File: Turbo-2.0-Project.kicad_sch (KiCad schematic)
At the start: 1 part, among them J1 Conn_01x02

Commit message: Update es32
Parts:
- added U1: ESP32-C3-WROOM-02, RF_Module:ESP32-C3-WROOM-02, symbol RF_Module:ESP32-C3-WROOM-02
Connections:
- new net: U1.19 (GND), U1.9 (GND)
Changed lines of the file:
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@@
+	)
+	(symbol
+		(lib_id "RF_Module:ESP32-C3-WROOM-02")
+		(at 102.87 60.96 0)
+		(unit 1)
+		(exclude_from_sim no)
+		(in_bom yes)
+		(on_board yes)
+		(dnp no)
+		(fields_autoplaced yes)
+		(property "Reference" "U1"
+			(at 105.0133 35.56 0)
+			(effects
+				(font
+					(size 1.27 1.27)
+				)
+				(justify left)
+			)
+		)
+		(property "Value" "ESP32-C3-WROOM-02"
+			(at 105.0133 38.1 0)
+			(effects
+				(font
+					(size 1.27 1.27)
+				)
+				(justify left)
+			)
+		)
+		(property "Footprint" "RF_Module:ESP32-C3-WROOM-02"
+			(at 102.87 60.325 0)
+			(effects
+				(font
+					(size 1.27 1.27)
+				)
+				(hide yes)
+			)
+		)
+		(property "Datasheet" "https://www.espressif.com/sites/default/files/documentation/esp32-c3-wroom-02_datasheet_en.pdf"
+			(at 102.87 60.325 0)
+			(effects
+				(font
+					(size 1.27 1.27)
+				)
+				(hide yes)
+			)
+		)
+		(property "Description" "802.11 b/g/n Wi­Fi and Bluetooth 5 module, ESP32­C3 SoC, RISC­V microprocessor, On-board antenna"
+			(at 102.87 60.325 0)
+			(effects
+				(font
+					(size 1.27 1.27)
+				)
+				(hide yes)
+			)
+		)
+		(pin "7"
+		)
+		(pin "4"
+		)
+		(pin "3"
+		)
+		(pin "19"
+		)
+		(pin "17"
+		)
+		(pin "9"
+		)
+		(pin "11"
+		)
+		(pin "12"
+		)
+		(pin "2"
+		)
+		(pin "1"
+		)
+		(pin "6"
+		)
+		(pin "5"
+		)
+		(pin "14"
+		)
+		(pin "13"
+		)
+		(pin "15"
+		)
+		(pin "18"
+		)
+		(pin "16"
+		)
+		(pin "8"
+		)
+		(pin "10"
+		)
+		(instances
+			(project ""
+				(path "/aed3ed38-84bd-46b2-8591-0345416ed942"
+					(reference "U1")
+					(unit 1)
+				)
+			)
+		)
 	)
 	(symbol

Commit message: Updat4re
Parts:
- added M1: Motor_Servo, symbol Motor:Motor_Servo
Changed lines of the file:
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@@
+	)
+	(symbol
+		(lib_id "Motor:Motor_Servo")
+		(at 143.51 104.14 0)
+		(unit 1)
+		(exclude_from_sim no)
+		(in_bom yes)
+		(on_board yes)
+		(dnp no)
+		(fields_autoplaced yes)
+		(property "Reference" "M1"
+			(at 152.4 102.4368 0)
+			(effects
+				(font
+					(size 1.27 1.27)
+				)
+				(justify left)
+			)
+		)
+		(property "Value" "Motor_Servo"
+			(at 152.4 104.9768 0)
+			(effects
+				(font
+					(size 1.27 1.27)
+				)
+				(justify left)
+			)
+		)
+		(property "Footprint" ""
+			(at 143.51 108.966 0)
+			(effects
+				(font
+					(size 1.27 1.27)
+				)
+				(hide yes)
+			)
+		)
+		(property "Datasheet" "http://forums.parallax.com/uploads/attachments/46831/74481.png"
+			(at 143.51 108.966 0)
+			(effects
+				(font
+					(size 1.27 1.27)
+				)
+				(hide yes)
+			)
+		)
+		(property "Description" "Servo Motor (Futaba, HiTec, JR connector)"
+			(at 143.51 104.14 0)
+			(effects
+				(font
+					(size 1.27 1.27)
+				)
+				(hide yes)
+			)
+		)
+		(pin "2"
+		)
+		(pin "3"
+		)
+		(pin "1"
+		)
+		(instances
+			(project ""
+				(path "/aed3ed38-84bd-46b2-8591-0345416ed942"
+					(reference "M1")
+					(unit 1)
+				)
+			)
+		)
 	)
 	(symbol

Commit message: duplicate
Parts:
- added J2: Conn_01x02, symbol Connector_Generic:Conn_01x02
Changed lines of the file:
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@@
+	)
+	(symbol
+		(lib_id "Connector_Generic:Conn_01x02")
+		(at 146.05 68.58 0)
+		(unit 1)
+		(exclude_from_sim no)
+		(in_bom yes)
+		(on_board yes)
+		(dnp no)
+		(fields_autoplaced yes)
+		(property "Reference" "J2"
+			(at 148.59 68.5799 0)
+			(effects
+				(font
+					(size 1.27 1.27)
+				)
+				(justify left)
+			)
+		)
+		(property "Value" "Conn_01x02"
+			(at 148.59 71.1199 0)
+			(effects
+				(font
+					(size 1.27 1.27)
+				)
+				(justify left)
+			)
+		)
+		(property "Footprint" ""
+			(at 146.05 68.58 0)
+			(effects
+				(font
+					(size 1.27 1.27)
+				)
+				(hide yes)
+			)
+		)
+		(property "Datasheet" "~"
+			(at 146.05 68.58 0)
+			(effects
+				(font
+					(size 1.27 1.27)
+				)
+				(hide yes)
+			)
+		)
+		(property "Description" "Generic connector, single row, 01x02, script generated (kicad-library-utils/schlib/autogen/connector/)"
+			(at 146.05 68.58 0)
+			(effects
+				(font
+					(size 1.27 1.27)
+				)
+				(hide yes)
+			)
+		)
+		(pin "2"
+		)
+		(pin "1"
+		)
+		(instances
+			(project "Turbo-2.0-Project"
+				(path "/aed3ed38-84bd-46b2-8591-0345416ed942"
+					(reference "J2")
+					(unit 1)
+				)
+			)
+		)
 	)
 	(symbol

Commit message: WHats up
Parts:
- removed J1, J2: Conn_01x02, symbol Connector_Generic:Conn_01x02
- removed M1: Motor_Servo, symbol Motor:Motor_Servo
- removed U1: ESP32-C3-WROOM-02, RF_Module:ESP32-C3-WROOM-02, symbol RF_Module:ESP32-C3-WROOM-02
- added J1, J4, J5: Conn_01x06, symbol Connector_Generic:Conn_01x06
- added J2, J3: Conn_01x04, symbol Connector_Generic:Conn_01x04
- added U1: ~, symbol Turbo_Custom_Library:ESP32S3_Mini_Zero
- added U2: ~, symbol Turbo_Custom_Library:DRV8833_Motor_Driver
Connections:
- new net: J2.4 (Pin_4), U1. (7)

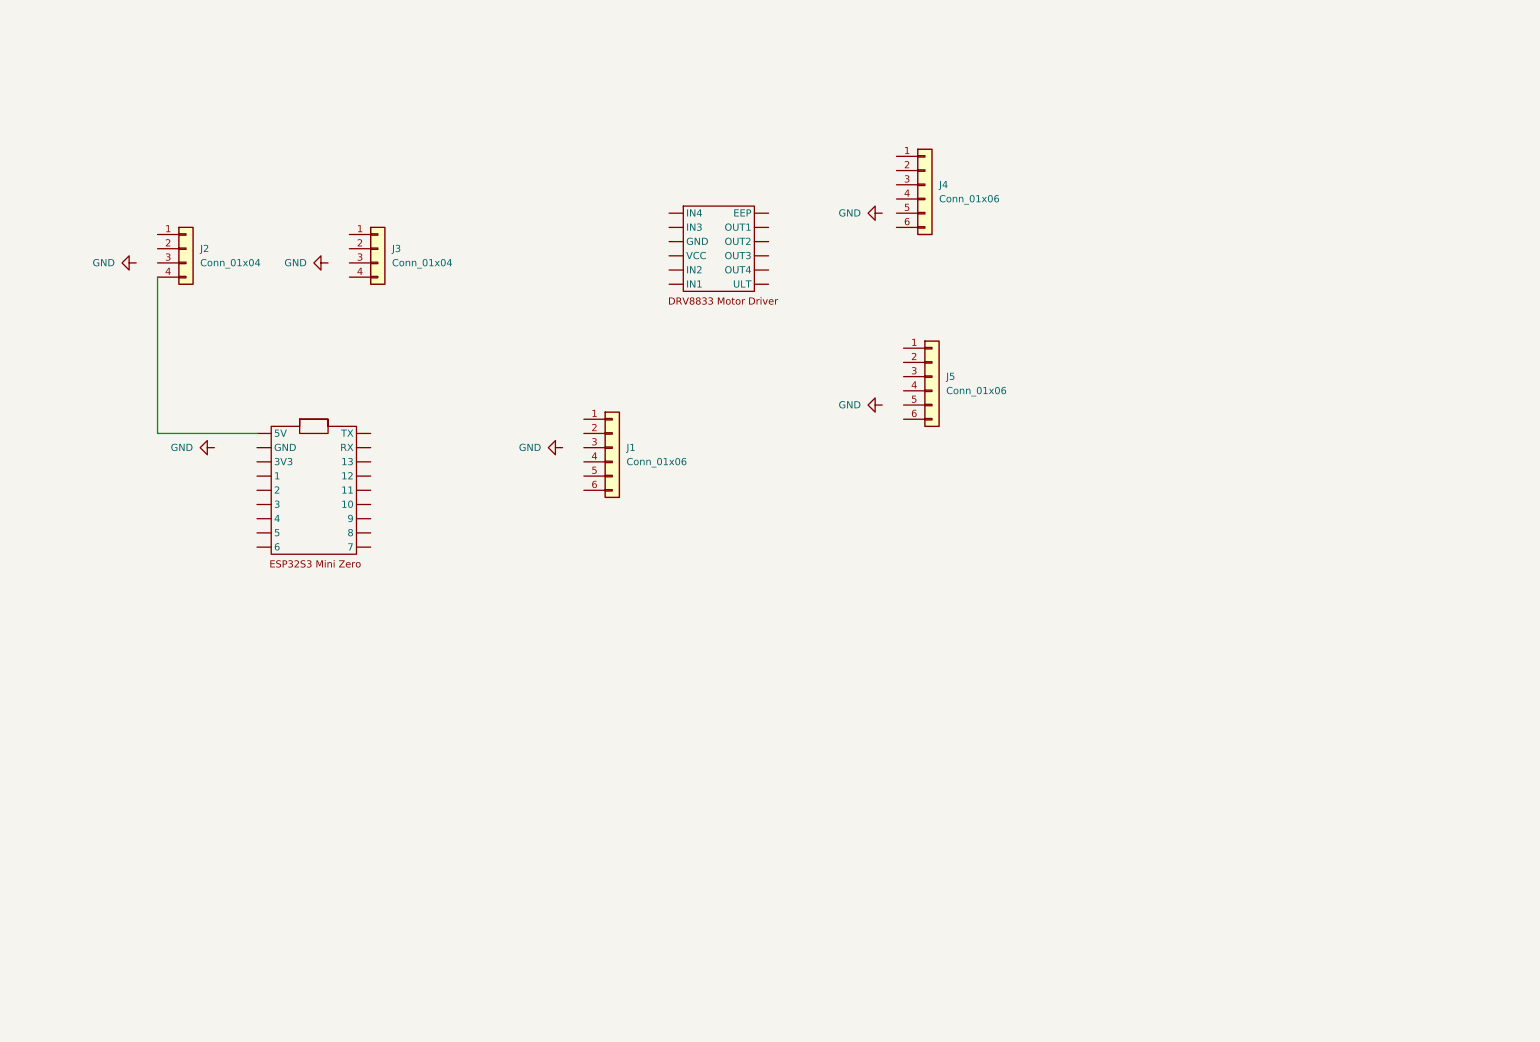
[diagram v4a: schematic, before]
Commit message: Completed Sensor and Emitter Circuitry
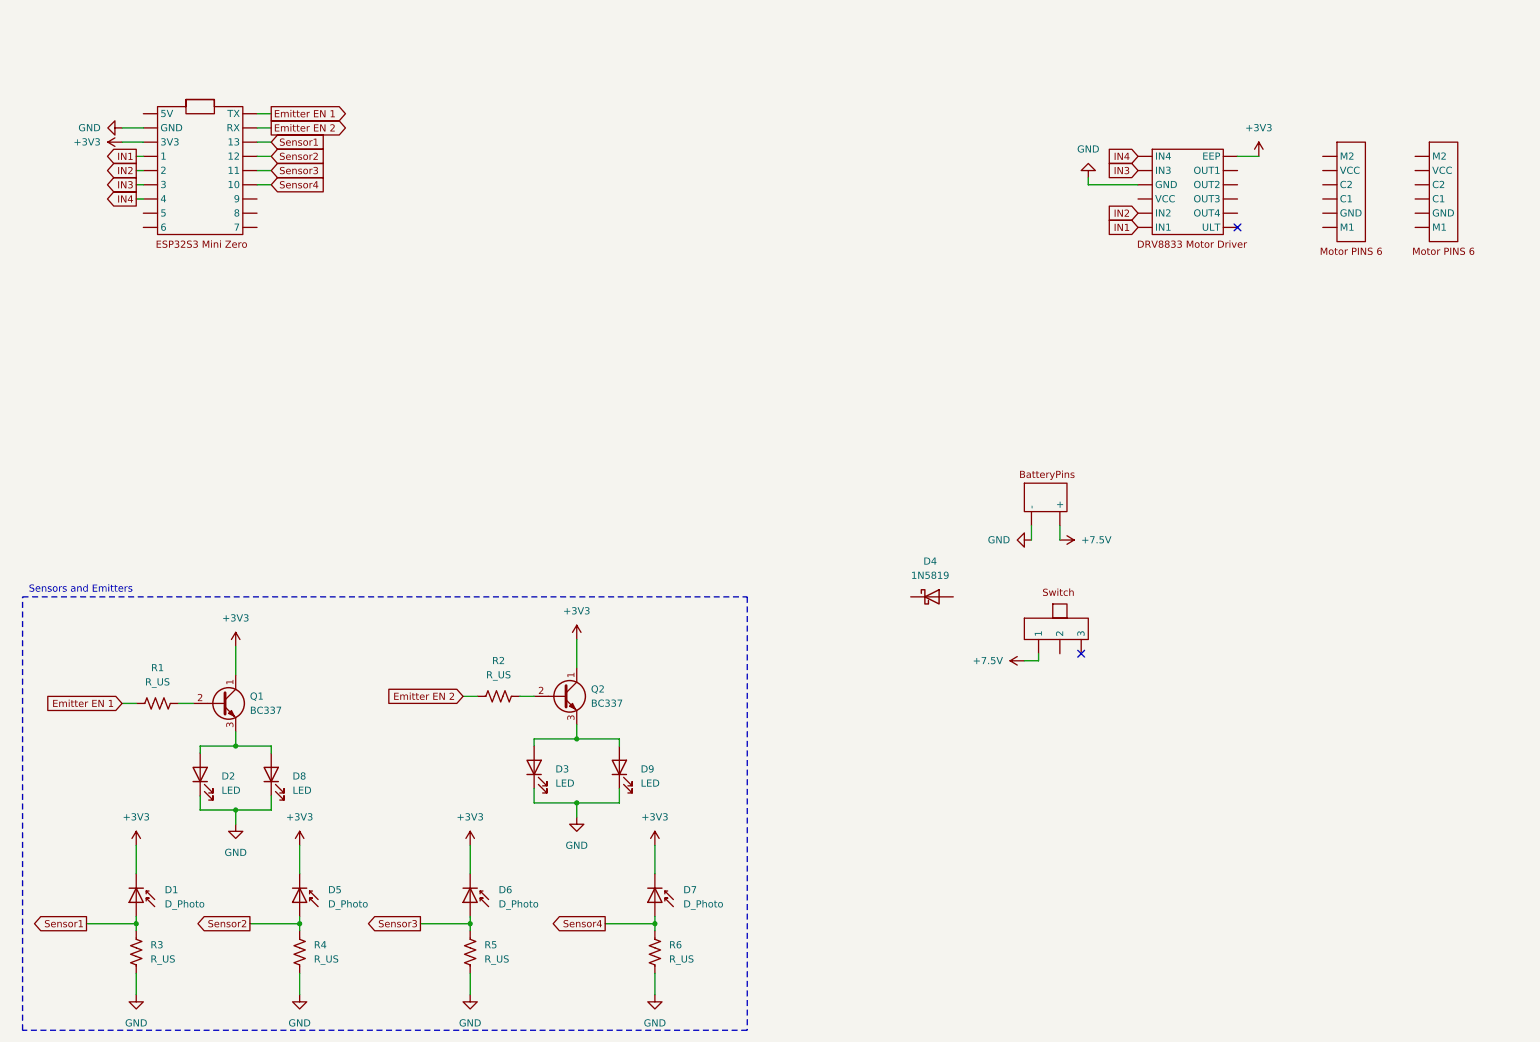
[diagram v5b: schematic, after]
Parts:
- removed J1, J4, J5: Conn_01x06, symbol Connector_Generic:Conn_01x06
- removed J2, J3: Conn_01x04, symbol Connector_Generic:Conn_01x04
- added D1, D5, D6, D7: D_Photo, symbol Device:D_Photo
- added D2, D3, D8, D9: LED, symbol Device:LED
- added D4: 1N5819, Diode_THT:D_DO-41_SOD81_P10.16mm_Horizontal, symbol Diode:1N5819
- added Q1, Q2: BC337, Package_TO_SOT_THT:TO-92_Inline, symbol Transistor_BJT:BC337
- added R1, R2, R3, R4, R5, R6: R_US, symbol Device:R_US
- added U3, U4: ~, symbol Turbo_Custom_Library:MotorPin6
- added U5: ~, symbol Turbo_Custom_Library:Battery
- added U6: ~, symbol Turbo_Custom_Library:Switch
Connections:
- net GND: now also U1. (7), U2. (ULT), D2.1 (K), D3.1 (K), D8.1 (K), D9.1 (K), R3.2, R4.2, R5.2, R6.2, U5. (+)
- net Sensor4: now reaches U1. (7)
- net Sensor4: now also D7.2 (A), R6.1
- net IN4: now reaches U2. (ULT)
- net IN4: now also U1. (7)
- new net: D2.2 (A), D8.2 (A), Q1.3 (E)
- new net: Q1.2 (B), R1.2
- new net: Q2.2 (B), R2.2
- new net: D3.2 (A), D9.2 (A), Q2.3 (E)
- new net +3V3: D1.1 (K), D5.1 (K), D6.1 (K), D7.1 (K), Q1.1 (C), Q2.1 (C), U1. (7), U2. (ULT)
- new net +7.5V: U5. (+), U6. (3)
- new net Emitter EN 1: R1.1, U1. (7)
- new net Emitter EN 2: R2.1, U1. (7)
- new net IN1: U1. (7), U2. (ULT)
- new net IN2: U1. (7), U2. (ULT)
- new net IN3: U1. (7), U2. (ULT)
- new net Sensor1: D1.2 (A), R3.1, U1. (7)
- new net Sensor2: D5.2 (A), R4.1, U1. (7)
- new net Sensor3: D6.2 (A), R5.1, U1. (7)
- no-connect marks 0 -> 2
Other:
- note added: "Sensors and Emitters"

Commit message: Wired Everything Up
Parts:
- added U7, U8: ~, symbol Turbo_Custom_Library:Step_down
- added U9: ~, symbol Turbo_Custom_Library:BNO085_IMU
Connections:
- net +3V3: now also U3. (M1), U4. (M1)
- net GND: now also U3. (M1), U4. (M1), U6. (3), U7. (Vo+), U8. (Vo+)
- net OUT2: now reaches U3. (M1)
- net OUT2: now also U2. (ULT), U4. (M1)
- net OUT4: now reaches U2. (ULT)
- net at D4.1 (K): now also U1. (7)
- net +5V: now reaches D4.2 (A)
- net +5V: now also U7. (Vo+)
- new net: U6. (3), U7. (Vo+), U8. (Vo+)
- new net +6V: U2. (ULT), U8. (Vo+)
- new net Motor1 C1: U1. (7), U3. (M1)
- new net Motor1 C2: U1. (7), U3. (M1)
- new net Motor2 C1: U1. (7), U4. (M1)
- new net Motor2 C2: U1. (7), U4. (M1)
- new net OUT1: U2. (ULT), U3. (M1), U4. (M1)
- new net OUT3: U2. (ULT)
- no-connect marks 2 -> 1
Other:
- note added: "Microcontroller"
- note added: "Motors and Driver"
- note added: "Power Circuitry"
- moved on the sheet: D1, D2, D3, D4, D5, D6, D7, D8, D9, Q1, Q2, R1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

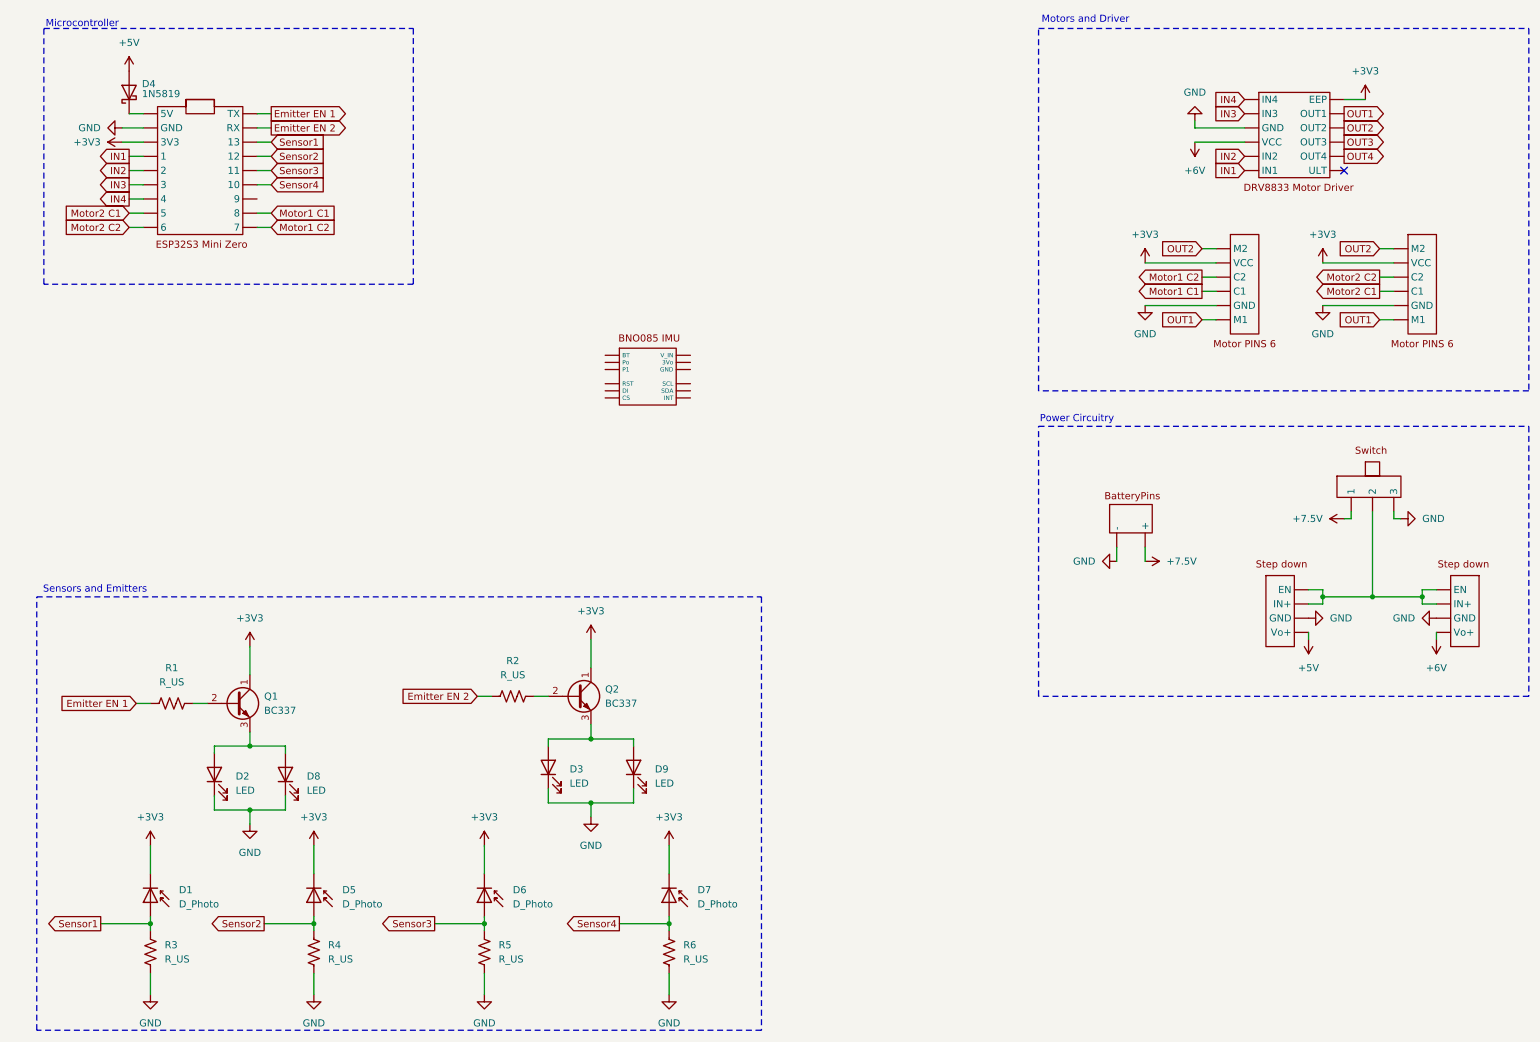
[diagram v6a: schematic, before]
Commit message: Added IMU to schematic
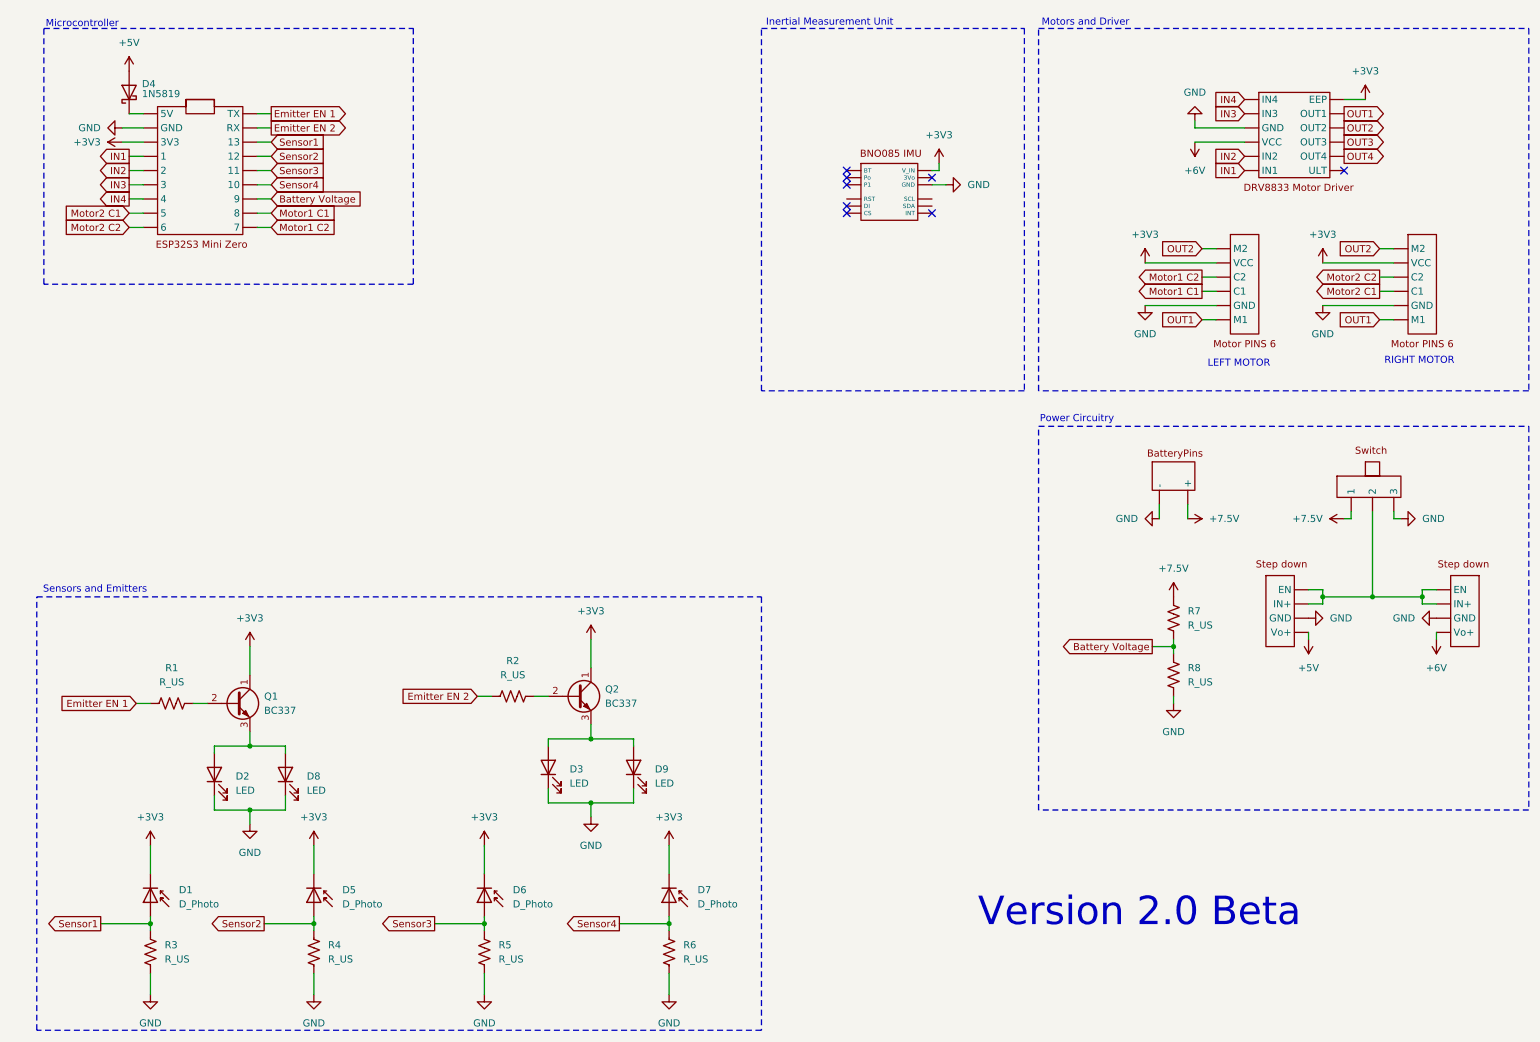
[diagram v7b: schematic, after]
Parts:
- added R7, R8: R_US, symbol Device:R_US
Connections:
- net +3V3: now also U9. (INT)
- net +7.5V: now also R7.1
- net GND: now also U9. (INT), R8.2
- new net: U6. (3), U7. (Vo+), U8. (Vo+)
- new net Battery Voltage: R7.2, R8.1, U1. (7)
- no-connect marks 1 -> 8
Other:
- note added: "Inertial Measurement Unit"
- note added: "LEFT MOTOR"
- note added: "RIGHT MOTOR"
- note added: "Version 2.0 Beta"

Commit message: ESP32 Footprint
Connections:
- new net: U6. (3), U7. (Vo+), U8. (Vo+)
